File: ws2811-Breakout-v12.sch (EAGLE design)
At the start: 9 parts, among them U1 LED-TRICOLOR-5050

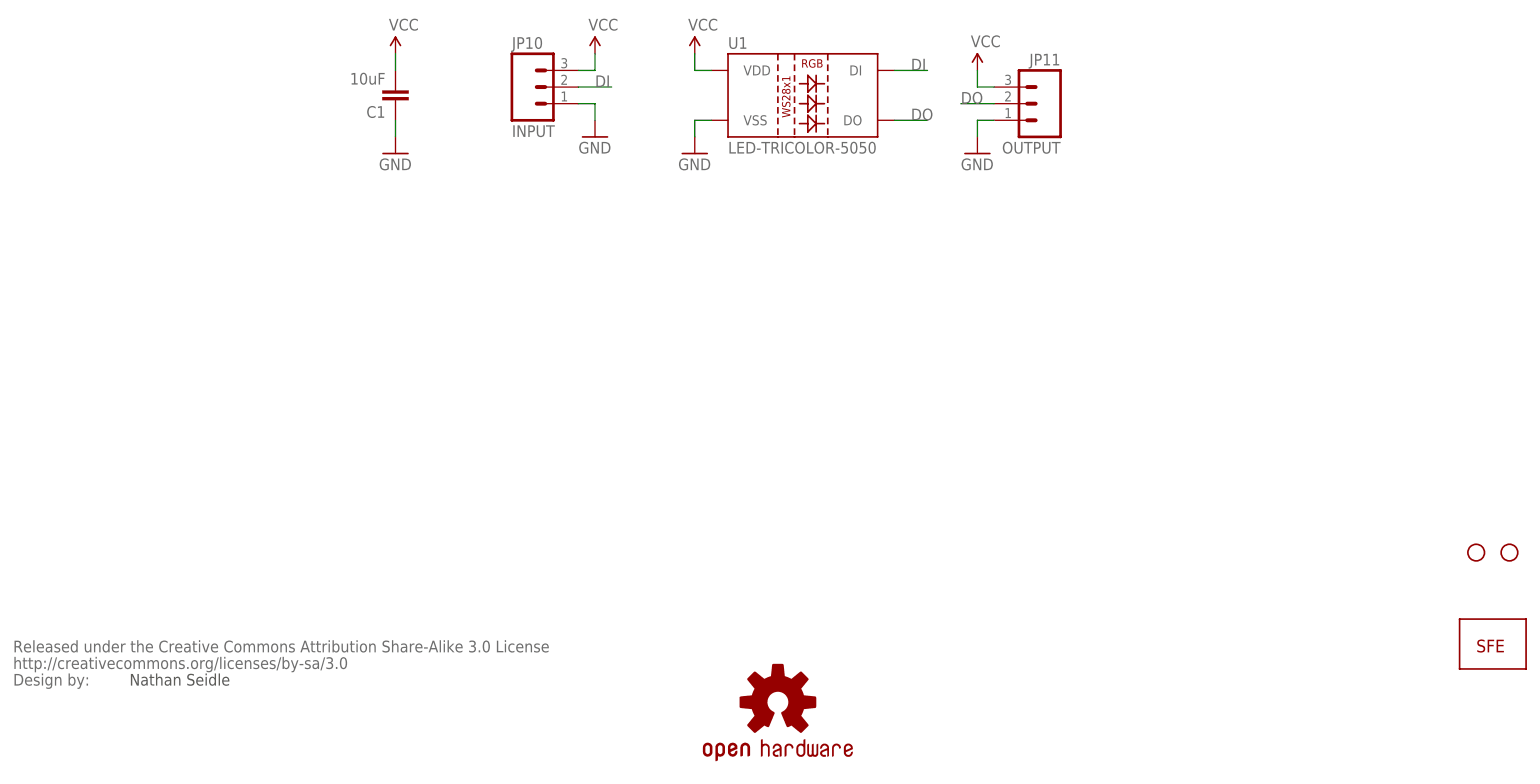
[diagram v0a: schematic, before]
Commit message: Fixed all erros posed by engineers
Changed dimension to allow board to fit on .1 grid.
Changed cap value and package.
Used new frame on sch.
Centered LED.
Clean up repo.
Added version code instead of date.
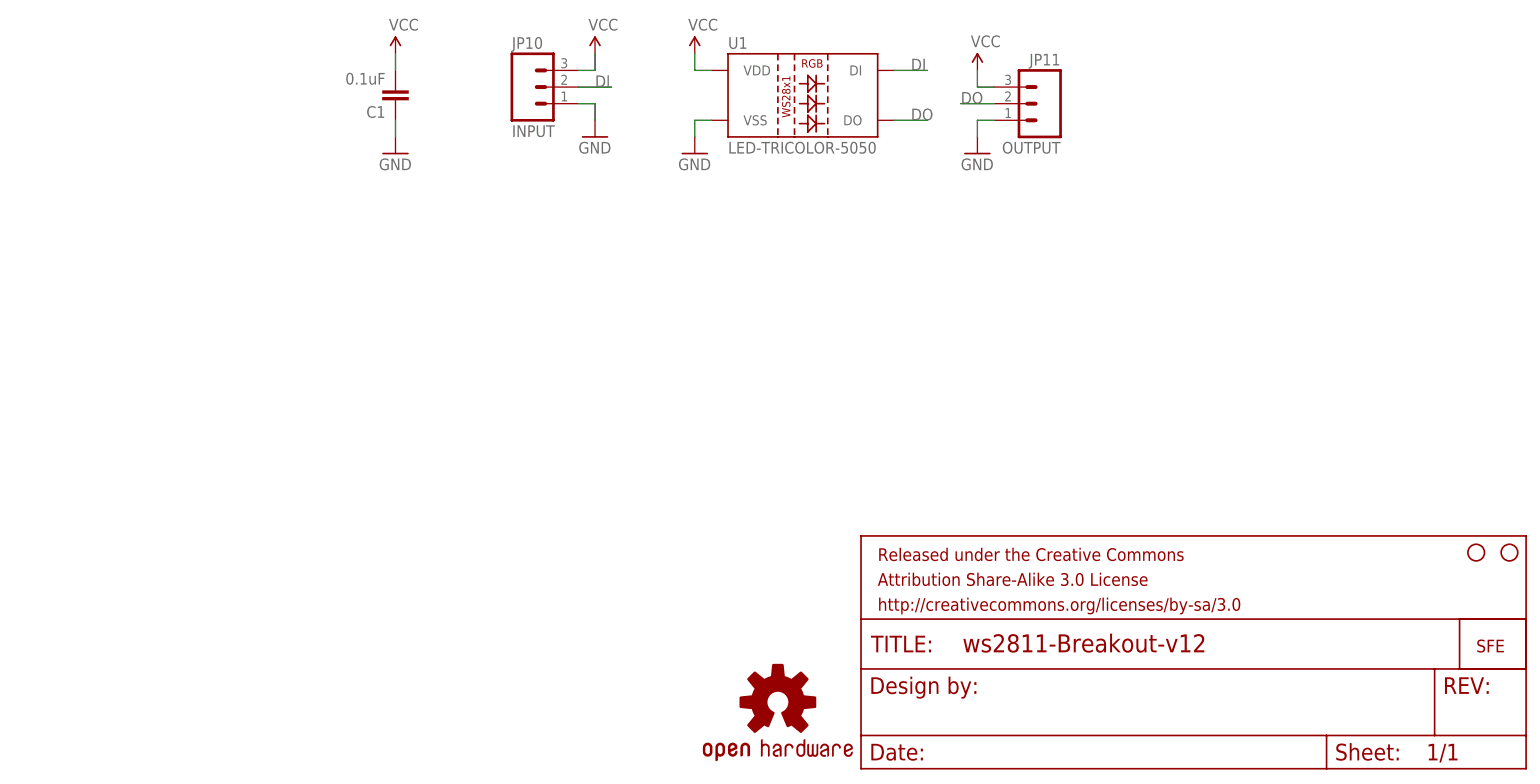
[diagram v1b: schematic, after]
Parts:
- removed U$1: CREATIVE_COMMONS, SparkFun:CREATIVE_COMMONS
- added FRAME2: FRAME-LETTER, SparkFun-Aesthetics:FRAME-LETTER
- C1: value 10uF -> 0.1uF; device SparkFun:CAP1206 -> SparkFun:CAP0603-CAP
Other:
- note removed: "Nathan Seidle"
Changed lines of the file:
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@@
 <grid distance="0.1" unitdist="inch" unit="inch" style="lines" multiple="1" display="no" altdistance="0.01" altunitdist="inch" altunit="inch"/>
 <layers>
-<layer number="1" name="Top" color="4" fill="1" visible="no" active="no"/>
-<layer number="2" name="Route2" color="1" fill="3" visible="no" active="no"/>
-<layer number="3" name="Route3" color="4" fill="3" visible="no" active="no"/>
-<layer number="4" name="Route4" color="1" fill="4" visible="no" active="no"/>
-<layer number="5" name="Route5" color="4" fill="4" visible="no" active="no"/>
-<layer number="6" name="Route6" color="1" fill="8" visible="no" active="no"/>
-<layer number="7" name="Route7" color="4" fill="8" visible="no" active="no"/>
-<layer number="8" name="Route8" color="1" fill="2" visible="no" active="no"/>
-<layer number="9" name="Route9" color="4" fill="2" visible="no" active="no"/>
-<layer number="10" name="Route10" color="1" fill="7" visible="no" active="no"/>
-<layer number="11" name="Route11" color="4" fill="7" visible="no" active="no"/>
-<layer number="12" name="Route12" color="1" fill="5" visible="no" active="no"/>
-<layer number="13" name="Route13" color="4" fill="5" visible="no" active="no"/>
-<layer number="14" name="Route14" color="1" fill="6" visible="no" active="no"/>
-<layer number="15" name="Route15" color="4" fill="6" visible="no" active="no"/>
-<layer number="16" name="Bottom" color="1" fill="1" visible="no" active="no"/>
-<layer number="17" name="Pads" color="2" fill="1" visible="no" active="no"/>
-<layer number="18" name="Vias" color="2" fill="1" visible="no" active="no"/>
-<layer number="19" name="Unrouted" color="6" fill="1" visible="no" active="no"/>
-<layer number="20" name="Dimension" color="6" fill="1" visible="no" active="no"/>
-<layer number="21" name="tPlace" color="6" fill="1" visible="no" active="no"/>
-<layer number="22" name="bPlace" color="6" fill="1" visible="no" active="no"/>
-<layer number="23" name="tOrigins" color="15" fill="1" visible="no" active="no"/>
-<layer number="24" name="bOrigins" color="15" fill="1" visible="no" active="no"/>
-<layer number="25" name="tNames" color="7" fill="1" visible="no" active="no"/>
-<layer number="26" name="bNames" color="7" fill="1" visible="no" active="no"/>
-<layer number="27" name="tValues" color="7" fill="1" visible="no" active="no"/>
-<layer number="28" name="bValues" color="7" fill="1" visible="no" active="no"/>
+<layer number="1" name="Top" color="4" fill="1" visible="yes" active="no"/>
+<layer number="2" name="Route2" color="1" fill="3" visible="yes" active="no"/>
+<layer number="3" name="Route3" color="4" fill="3" visible="yes" active="no"/>
+<layer number="4" name="Route4" color="1" fill="4" visible="yes" active="no"/>
+<layer number="5" name="Route5" color="4" fill="4" visible="yes" active="no"/>
+<layer number="6" name="Route6" color="1" fill="8" visible="yes" active="no"/>
+<layer number="7" name="Route7" color="4" fill="8" visible="yes" active="no"/>
+<layer number="8" name="Route8" color="1" fill="2" visible="yes" active="no"/>
+<layer number="9" name="Route9" color="4" fill="2" visible="yes" active="no"/>
+<layer number="10" name="Route10" color="1" fill="7" visible="yes" active="no"/>
+<layer number="11" name="Route11" color="4" fill="7" visible="yes" active="no"/>
+<layer number="12" name="Route12" color="1" fill="5" visible="yes" active="no"/>
+<layer number="13" name="Route13" color="4" fill="5" visible="yes" active="no"/>
+<layer number="14" name="Route14" color="1" fill="6" visible="yes" active="no"/>
+<layer number="15" name="Route15" color="4" fill="6" visible="yes" active="no"/>
+<layer number="16" name="Bottom" color="1" fill="1" visible="yes" active="no"/>
+<layer number="17" name="Pads" color="2" fill="1" visible="yes" active="no"/>
+<layer number="18" name="Vias" color="2" fill="1" visible="yes" active="no"/>
+<layer number="19" name="Unrouted" color="6" fill="1" visible="yes" active="no"/>
+<layer number="20" name="Dimension" color="7" fill="1" visible="yes" active="no"/>
+<layer number="21" name="tPlace" color="16" fill="1" visible="yes" active="no"/>
+<layer number="22" name="bPlace" color="14" fill="1" visible="yes" active="no"/>
+<layer number="23" name="tOrigins" color="15" fill="1" visible="yes" active="no"/>
+<layer number="24" name="bOrigins" color="15" fill="1" visible="yes" active="no"/>
+<layer number="25" name="tNames" color="7" fill="1" visible="yes" active="no"/>
+<layer number="26" name="bNames" color="7" fill="1" visible="yes" active="no"/>
+<layer number="27" name="tValues" color="7" fill="1" visible="yes" active="no"/>
+<layer number="28" name="bValues" color="7" fill="1" visible="yes" active="no"/>
 <layer number="29" name="tStop" color="7" fill="3" visible="no" active="no"/>
 <layer number="30" name="bStop" color="7" fill="6" visible="no" active="no"/>
@@
 <layer number="35" name="tGlue" color="7" fill="4" visible="no" active="no"/>
 <layer number="36" name="bGlue" color="7" fill="5" visible="no" active="no"/>
-<layer number="37" name="tTest" color="7" fill="1" visible="no" active="no"/>
-<layer number="38" name="bTest" color="7" fill="1" visible="no" active="no"/>
+<layer number="37" name="tTest" color="7" fill="1" visible="yes" active="no"/>
+<layer number="38" name="bTest" color="7" fill="1" visible="yes" active="no"/>
 <layer number="39" name="tKeepout" color="4" fill="11" visible="no" active="no"/>
 <layer number="40" name="bKeepout" color="1" fill="11" visible="no" active="no"/>
@@
 <layer number="44" name="Drills" color="7" fill="1" visible="no" active="no"/>
 <layer number="45" name="Holes" color="7" fill="1" visible="no" active="no"/>
-<layer number="46" name="Milling" color="3" fill="1" visible="no" active="no"/>
-<layer number="47" name="Measures" color="7" fill="1" visible="no" active="no"/>
-<layer number="48" name="Document" color="7" fill="1" visible="no" active="no"/>
-<layer number="49" name="Reference" color="7" fill="1" visible="no" active="no"/>
-<layer number="50" name="dxf" color="7" fill="1" visible="no" active="no"/>
-<layer number="51" name="tDocu" color="6" fill="1" visible="no" active="no"/>
-<layer number="52" name="bDocu" color="7" fill="1" visible="no" active="no"/>
-<layer number="53" name="tGND_GNDA" color="7" fill="9" visible="no" active="no"/>
-<layer number="54" name="bGND_GNDA" color="1" fill="9" visible="no" active="no"/>
-<layer number="56" name="wert" color="7" fill="1" visible="no" active="no"/>
+<layer number="46" name="Milling" color="3" fill="1" visible="yes" active="no"/>
+<layer number="47" name="Measures" color="7" fill="1" visible="yes" active="no"/>
+<layer number="48" name="Document" color="7" fill="1" visible="yes" active="no"/>
+<layer number="49" name="Reference" color="7" fill="1" visible="yes" active="no"/>
+<layer number="50" name="dxf" color="7" fill="1" visible="yes" active="no"/>
+<layer number="51" name="tDocu" color="6" fill="1" visible="yes" active="no"/>
+<layer number="52" name="bDocu" color="7" fill="1" visible="yes" active="no"/>
+<layer number="53" name="tGND_GNDA" color="7" fill="9" visible="yes" active="no"/>
+<layer number="54" name="bGND_GNDA" color="1" fill="9" visible="yes" active="no"/>
+<layer number="56" name="wert" color="7" fill="1" visible="yes" active="no"/>
 <layer number="91" name="Nets" color="2" fill="1" visible="yes" active="yes"/>
 <layer number="92" name="Busses" color="1" fill="1" visible="yes" active="yes"/>
@@
 <part name="P+1" library="SparkFun" deviceset="VCC" device=""/>
 <part name="GND1" library="SparkFun" deviceset="GND" device=""/>
-<part name="C1" library="SparkFun" deviceset="CAP" device="1206" value="10uF"/>
+<part name="C1" library="SparkFun" deviceset="CAP" device="0603-CAP" value="0.1uF"/>
 <part name="JP3" library="SparkFun" deviceset="LOGO-SFE" device="SK"/>
-<part name="U$1" library="SparkFun" deviceset="CREATIVE_COMMONS" device=""/>
 <part name="JP1" library="SparkFun" deviceset="STAND-OFF" device=""/>
 <part name="JP4" library="SparkFun" deviceset="STAND-OFF" device=""/>
@@
 <part name="GND4" library="SparkFun" deviceset="GND" device=""/>
 <part name="LOGO1" library="SparkFun-Aesthetics" deviceset="OSHW-LOGO" device="S"/>
+<part name="FRAME2" library="SparkFun-Aesthetics" deviceset="FRAME-LETTER" device=""/>
 </parts>
 <sheets>
 <sheet>
 <plain>
-<text x="35.56" y="12.7" size="1.778" layer="97">Nathan Seidle</text>
 </plain>
 <instances>
@@
 <instance part="C1" gate="G$1" x="76.2" y="104.14" rot="R180"/>
 <instance part="JP3" gate="G$1" x="241.3" y="17.78"/>
-<instance part="U$1" gate="G$1" x="17.78" y="12.7"/>
 <instance part="JP1" gate="G$1" x="246.38" y="33.02"/>
 <instance part="JP4" gate="G$1" x="241.3" y="33.02"/>
@@
 <instance part="GND4" gate="1" x="165.1" y="93.98"/>
 <instance part="LOGO1" gate="G$1" x="134.62" y="10.16"/>
+<instance part="FRAME2" gate="G$2" x="147.32" y="0"/>
 </instances>
 <busses>
